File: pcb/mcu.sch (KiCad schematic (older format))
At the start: 7 parts

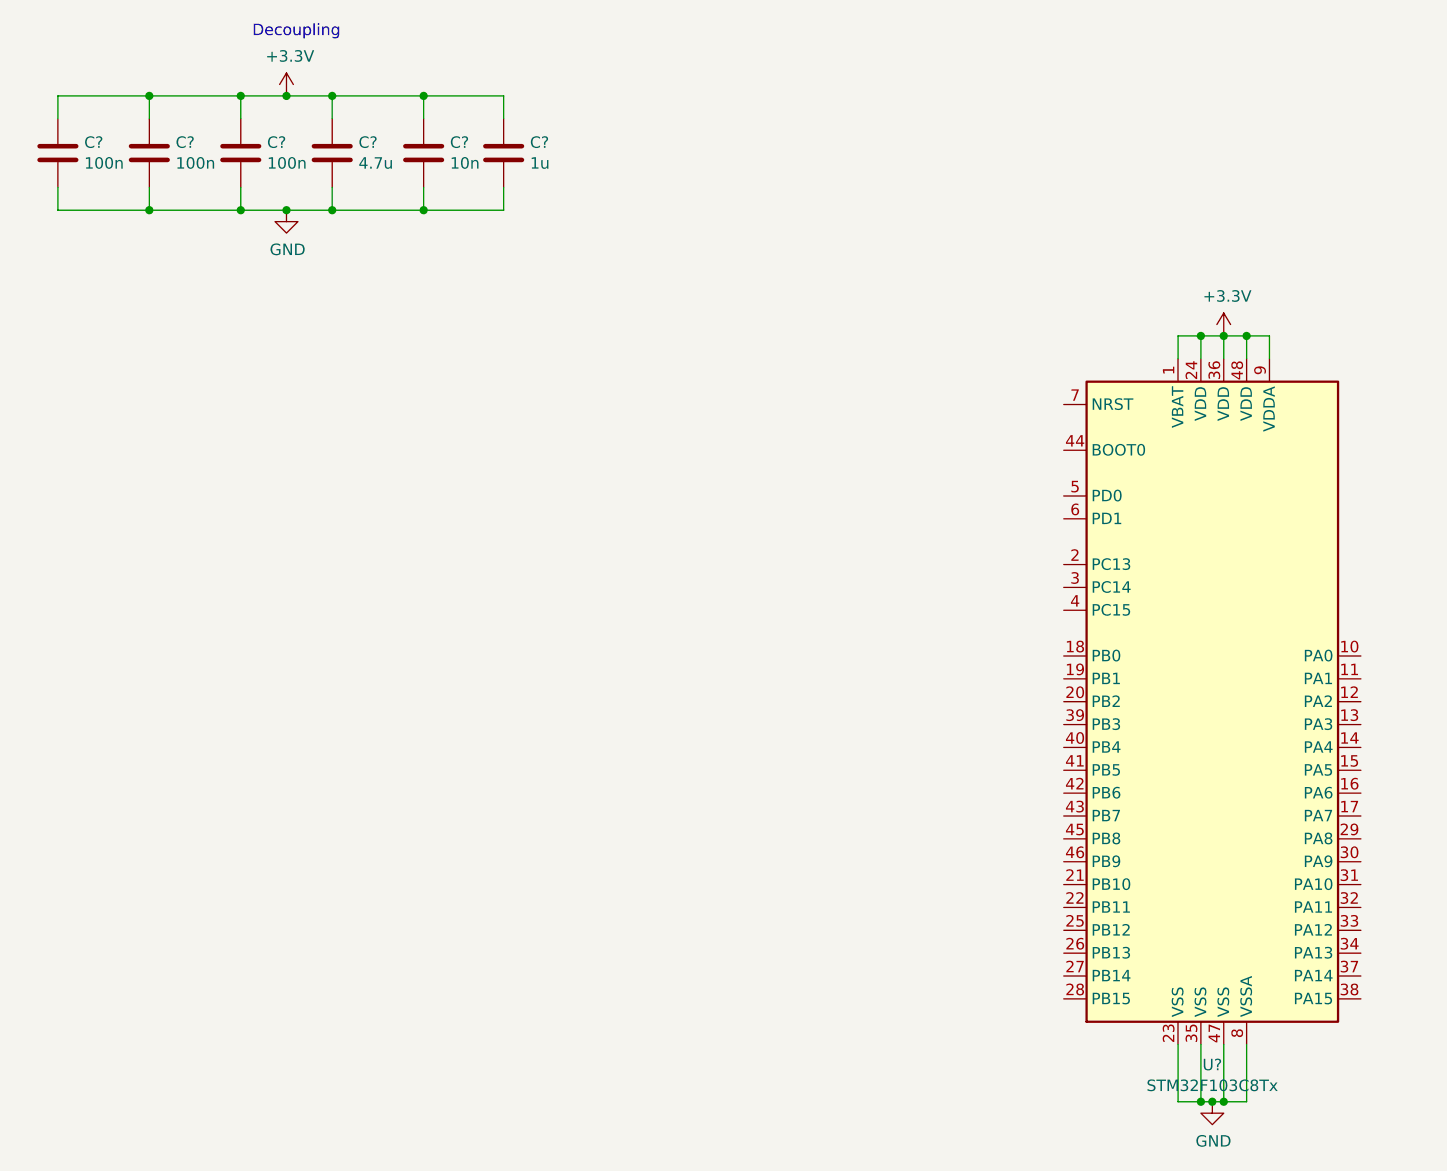
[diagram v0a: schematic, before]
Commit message: [PCB] MCU Crystal
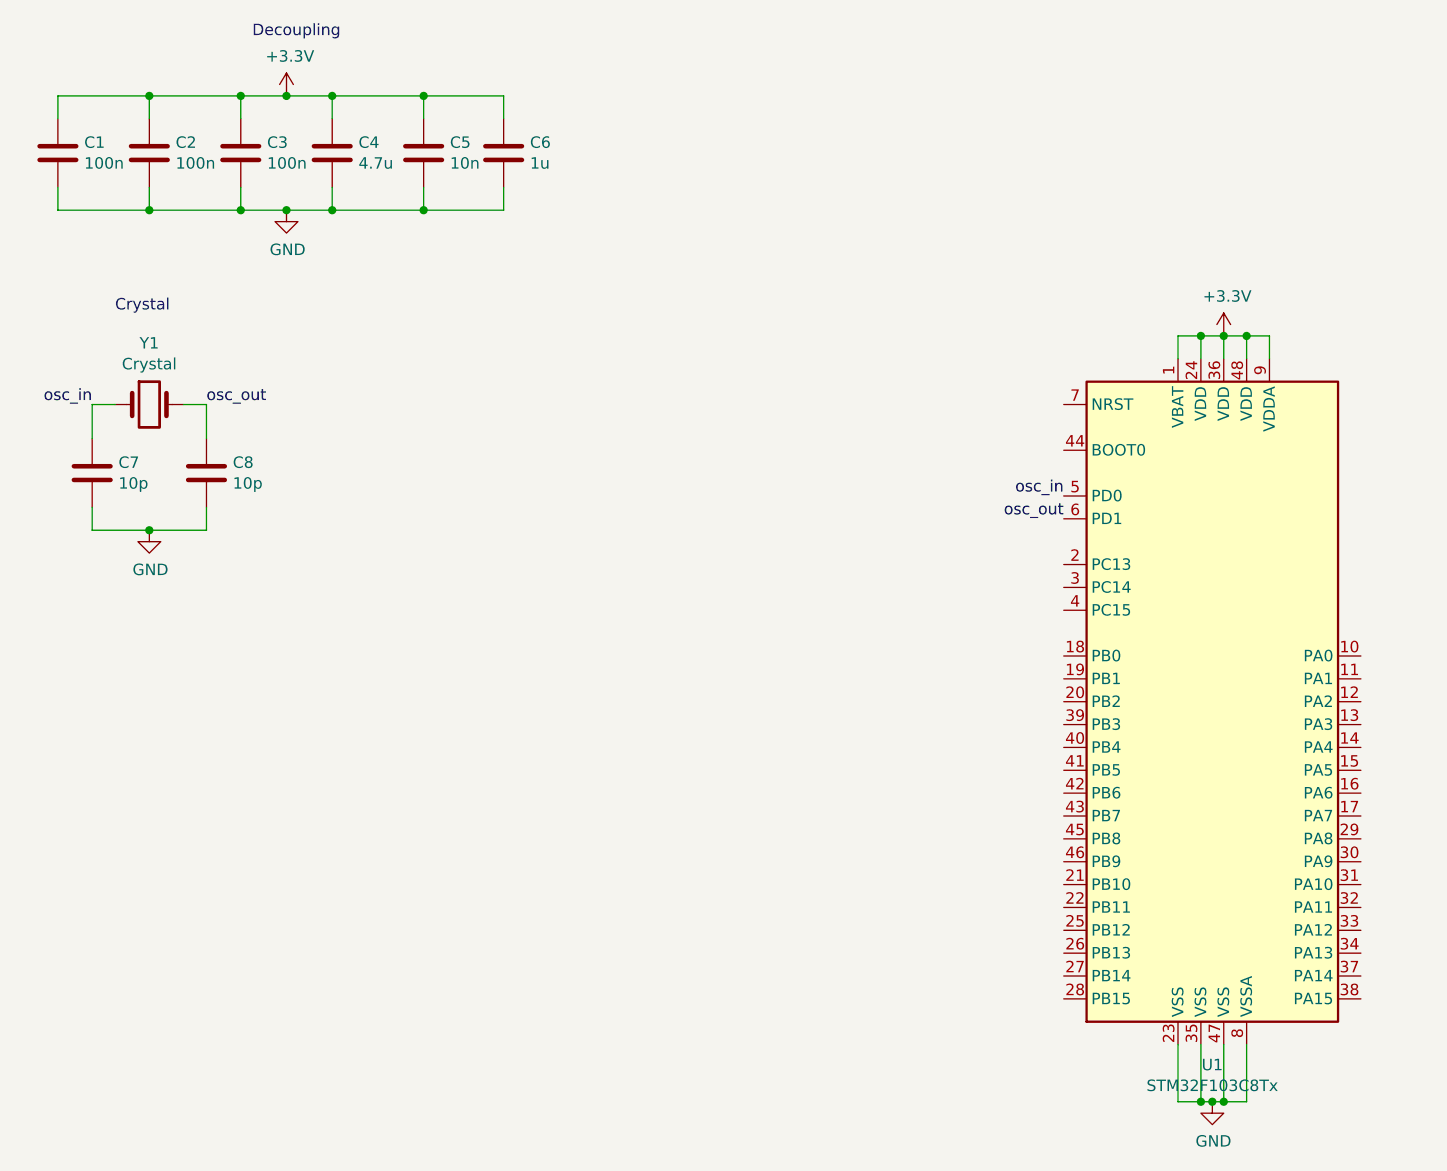
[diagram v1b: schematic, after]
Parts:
- added C7, C8: 10p, symbol Device:C
- added Y1: Crystal, symbol Device:Crystal
- gave numbers to parts that had none: 7
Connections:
- net GND: now also C7.2, C8.2
- net osc_in: now reaches U1.5 (PD0)
- net osc_in: now also C7.1, Y1.1
- net osc_out: now reaches U1.6 (PD1)
- net osc_out: now also C8.1, Y1.2
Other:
- note added: "Crystal"
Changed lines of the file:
@@
 $EndDescr
 $Comp
-L MCU_ST_STM32F1:STM32F103C8Tx U?
+L MCU_ST_STM32F1:STM32F103C8Tx U1
 U 1 1 5D0AE0C1
 P 5750 3500
-F 0 "U?" H 5700 1911 50  0000 C CNN
+F 0 "U1" H 5700 1911 50  0000 C CNN
 F 1 "STM32F103C8Tx" H 5700 1820 50  0000 C CNN
 F 2 "Package_QFP:LQFP-48_7x7mm_P0.5mm" H 5150 2100 50  0001 R CNN
@@
 $EndComp
 $Comp
-L power:GND #PWR?
+L power:GND #PWR05
 U 1 1 5D0B3E48
 P 5700 5250
-F 0 "#PWR?" H 5700 5000 50  0001 C CNN
+F 0 "#PWR05" H 5700 5000 50  0001 C CNN
 F 1 "GND" H 5705 5077 50  0000 C CNN
 F 2 "" H 5700 5250 50  0001 C CNN
@@
 Decoupling
 $Comp
-L power:+3.3V #PWR?
+L power:+3.3V #PWR01
 U 1 1 5D0BC77C
 P 1650 850
-F 0 "#PWR?" H 1650 700 50  0001 C CNN
+F 0 "#PWR01" H 1650 700 50  0001 C CNN
 F 1 "+3.3V" H 1665 1023 50  0000 C CNN
 F 2 "" H 1650 850 50  0001 C CNN
@@
 $EndComp
 $Comp
-L Device:C C?
+L Device:C C1
 U 1 1 5D0BCC7C
 P 650 1100
-F 0 "C?" H 765 1146 50  0000 L CNN
+F 0 "C1" H 765 1146 50  0000 L CNN
 F 1 "100n" H 765 1055 50  0000 L CNN
 F 2 "" H 688 950 50  0001 C CNN
@@
 $EndComp
 $Comp
-L Device:C C?
+L Device:C C2
 U 1 1 5D0BD12F
 P 1050 1100
-F 0 "C?" H 1165 1146 50  0000 L CNN
+F 0 "C2" H 1165 1146 50  0000 L CNN
 F 1 "100n" H 1165 1055 50  0000 L CNN
 F 2 "" H 1088 950 50  0001 C CNN
@@
 $EndComp
 $Comp
-L Device:C C?
+L Device:C C3
 U 1 1 5D0BD74C
 P 1450 1100
-F 0 "C?" H 1565 1146 50  0000 L CNN
+F 0 "C3" H 1565 1146 50  0000 L CNN
 F 1 "100n" H 1565 1055 50  0000 L CNN
 F 2 "" H 1488 950 50  0001 C CNN
@@
 	5750 1900 5650 1900
 $Comp
-L power:+3.3V #PWR?
+L power:+3.3V #PWR03
 U 1 1 5D0AFF21
 P 5750 1900
-F 0 "#PWR?" H 5750 1750 50  0001 C CNN
+F 0 "#PWR03" H 5750 1750 50  0001 C CNN
 F 1 "+3.3V" H 5765 2073 50  0000 C CNN
 F 2 "" H 5750 1900 50  0001 C CNN
@@
 	5700 5250 5650 5250
 $Comp
-L Device:C C?
+L Device:C C4
 U 1 1 5D0C6E4D
 P 1850 1100
-F 0 "C?" H 1965 1146 50  0000 L CNN
+F 0 "C4" H 1965 1146 50  0000 L CNN
 F 1 "4.7u" H 1965 1055 50  0000 L CNN
 F 2 "" H 1888 950 50  0001 C CNN
@@
 $EndComp
 $Comp
-L Device:C C?
+L Device:C C5
 U 1 1 5D0C8182
 P 2250 1100
-F 0 "C?" H 2365 1146 50  0000 L CNN
+F 0 "C5" H 2365 1146 50  0000 L CNN
 F 1 "10n" H 2365 1055 50  0000 L CNN
 F 2 "" H 2288 950 50  0001 C CNN
@@
 $EndComp
 $Comp
-L Device:C C?
+L Device:C C6
 U 1 1 5D0C8C05
 P 2600 1100
-F 0 "C?" H 2715 1146 50  0000 L CNN
+F 0 "C6" H 2715 1146 50  0000 L CNN
 F 1 "1u" H 2715 1055 50  0000 L CNN
 F 2 "" H 2638 950 50  0001 C CNN
@@
 	2250 850  1850 850
 $Comp
-L power:GND #PWR?
+L power:GND #PWR02
 U 1 1 5D0D37FC
 P 1650 1350
-F 0 "#PWR?" H 1650 1100 50  0001 C CNN
+F 0 "#PWR02" H 1650 1100 50  0001 C CNN
 F 1 "GND" H 1655 1177 50  0000 C CNN
 F 2 "" H 1650 1350 50  0001 C CNN
@@
 Wire Wire Line
 	1850 1350 2250 1350
+Text Notes 900  1800 0    50   ~ 0
+Crystal
+$Comp
+L Device:Crystal Y1
+U 1 1 5D0DE5C2
+P 1050 2200
+F 0 "Y1" H 1050 2468 50  0000 C CNN
+F 1 "Crystal" H 1050 2377 50  0000 C CNN
+F 2 "" H 1050 2200 50  0001 C CNN
+F 3 "~" H 1050 2200 50  0001 C CNN
+	1    1050 2200
+	1    0    0    -1
+$EndComp
+$Comp
+L power:GND #PWR04
+U 1 1 5D0DEFF9
+P 1050 2750
+F 0 "#PWR04" H 1050 2500 50  0001 C CNN
+F 1 "GND" H 1055 2577 50  0000 C CNN
+F 2 "" H 1050 2750 50  0001 C CNN
+F 3 "" H 1050 2750 50  0001 C CNN
+	1    1050 2750
+	1    0    0    -1
+$EndComp
+$Comp
+L Device:C C7
+U 1 1 5D0DF7DE
+P 800 2500
+F 0 "C7" H 915 2546 50  0000 L CNN
+F 1 "10p" H 915 2455 50  0000 L CNN
+F 2 "" H 838 2350 50  0001 C CNN
+F 3 "~" H 800 2500 50  0001 C CNN
+	1    800  2500
+	1    0    0    -1
+$EndComp
+$Comp
+L Device:C C8
+U 1 1 5D0DFE7A
+P 1300 2500
+F 0 "C8" H 1415 2546 50  0000 L CNN
+F 1 "10p" H 1415 2455 50  0000 L CNN
+F 2 "" H 1338 2350 50  0001 C CNN
+F 3 "~" H 1300 2500 50  0001 C CNN
+	1    1300 2500
+	1    0    0    -1
+$EndComp
+Wire Wire Line
+	800  2650 800  2750
+Wire Wire Line
+	800  2750 1050 2750
+Wire Wire Line
+	1300 2650 1300 2750
+Wire Wire Line
+	1300 2750 1050 2750
+Connection ~ 1050 2750
+Wire Wire Line
+	800  2350 800  2200
+Wire Wire Line
+	800  2200 900  2200
+Wire Wire Line
+	1200 2200 1300 2200
+Wire Wire Line
+	1300 2200 1300 2350
+Text Label 800  2200 2    50   ~ 0
+osc_in
+Text Label 1300 2200 0    50   ~ 0
+osc_out
+Text Label 5050 2600 2    50   ~ 0
+osc_in
+Text Label 5050 2700 2    50   ~ 0
+osc_out
 $EndSCHEMATC

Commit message: [PCB] Assign Footprints
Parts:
- C1, C2, C3, C4, C5, C6, C7, C8: footprint (none) -> Capacitor_SMD:C_0805_2012Metric
- Y1: footprint (none) -> Crystal:Crystal_SMD_HC49-SD
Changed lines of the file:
@@
 F 0 "C1" H 765 1146 50  0000 L CNN
 F 1 "100n" H 765 1055 50  0000 L CNN
-F 2 "" H 688 950 50  0001 C CNN
+F 2 "Capacitor_SMD:C_0805_2012Metric" H 688 950 50  0001 C CNN
 F 3 "~" H 650 1100 50  0001 C CNN
 	1    650  1100
@@
 F 0 "C2" H 1165 1146 50  0000 L CNN
 F 1 "100n" H 1165 1055 50  0000 L CNN
-F 2 "" H 1088 950 50  0001 C CNN
+F 2 "Capacitor_SMD:C_0805_2012Metric" H 1088 950 50  0001 C CNN
 F 3 "~" H 1050 1100 50  0001 C CNN
 	1    1050 1100
@@
 F 0 "C3" H 1565 1146 50  0000 L CNN
 F 1 "100n" H 1565 1055 50  0000 L CNN
-F 2 "" H 1488 950 50  0001 C CNN
+F 2 "Capacitor_SMD:C_0805_2012Metric" H 1488 950 50  0001 C CNN
 F 3 "~" H 1450 1100 50  0001 C CNN
 	1    1450 1100
@@
 F 0 "C4" H 1965 1146 50  0000 L CNN
 F 1 "4.7u" H 1965 1055 50  0000 L CNN
-F 2 "" H 1888 950 50  0001 C CNN
+F 2 "Capacitor_SMD:C_0805_2012Metric" H 1888 950 50  0001 C CNN
 F 3 "~" H 1850 1100 50  0001 C CNN
 	1    1850 1100
@@
 F 0 "C5" H 2365 1146 50  0000 L CNN
 F 1 "10n" H 2365 1055 50  0000 L CNN
-F 2 "" H 2288 950 50  0001 C CNN
+F 2 "Capacitor_SMD:C_0805_2012Metric" H 2288 950 50  0001 C CNN
 F 3 "~" H 2250 1100 50  0001 C CNN
 	1    2250 1100
@@
 F 0 "C6" H 2715 1146 50  0000 L CNN
 F 1 "1u" H 2715 1055 50  0000 L CNN
-F 2 "" H 2638 950 50  0001 C CNN
+F 2 "Capacitor_SMD:C_0805_2012Metric" H 2638 950 50  0001 C CNN
 F 3 "~" H 2600 1100 50  0001 C CNN
 	1    2600 1100
@@
 F 0 "Y1" H 1050 2468 50  0000 C CNN
 F 1 "Crystal" H 1050 2377 50  0000 C CNN
-F 2 "" H 1050 2200 50  0001 C CNN
+F 2 "Crystal:Crystal_SMD_HC49-SD" H 1050 2200 50  0001 C CNN
 F 3 "~" H 1050 2200 50  0001 C CNN
 	1    1050 2200
@@
 F 0 "C7" H 915 2546 50  0000 L CNN
 F 1 "10p" H 915 2455 50  0000 L CNN
-F 2 "" H 838 2350 50  0001 C CNN
+F 2 "Capacitor_SMD:C_0805_2012Metric" H 838 2350 50  0001 C CNN
 F 3 "~" H 800 2500 50  0001 C CNN
 	1    800  2500
@@
 F 0 "C8" H 1415 2546 50  0000 L CNN
 F 1 "10p" H 1415 2455 50  0000 L CNN
-F 2 "" H 1338 2350 50  0001 C CNN
+F 2 "Capacitor_SMD:C_0805_2012Metric" H 1338 2350 50  0001 C CNN
 F 3 "~" H 1300 2500 50  0001 C CNN
 	1    1300 2500
